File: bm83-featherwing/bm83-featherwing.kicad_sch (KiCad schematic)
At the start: 19 parts, among them J1 TOP, J2 BOT, J3 DX07S016JA1R1500, SW1 Reset Switch, SW2 Power Switch, U1 BM83SM1-00AA

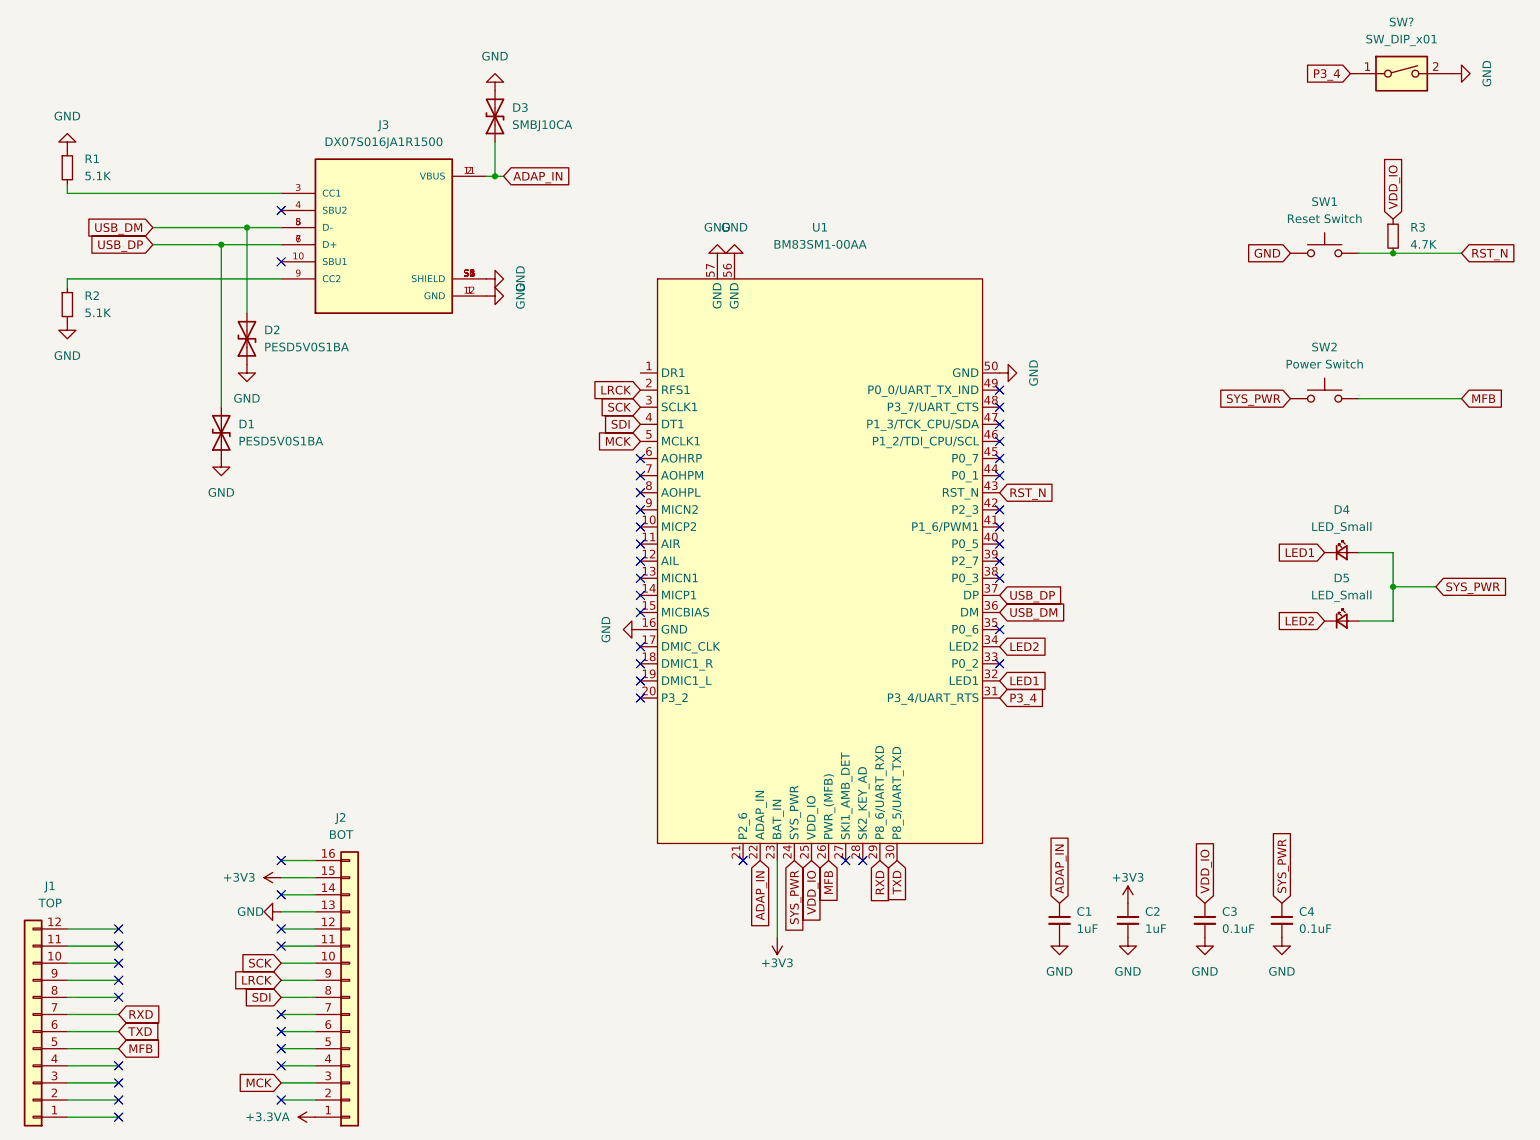
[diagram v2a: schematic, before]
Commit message: BM83 board first route. Needs labelling
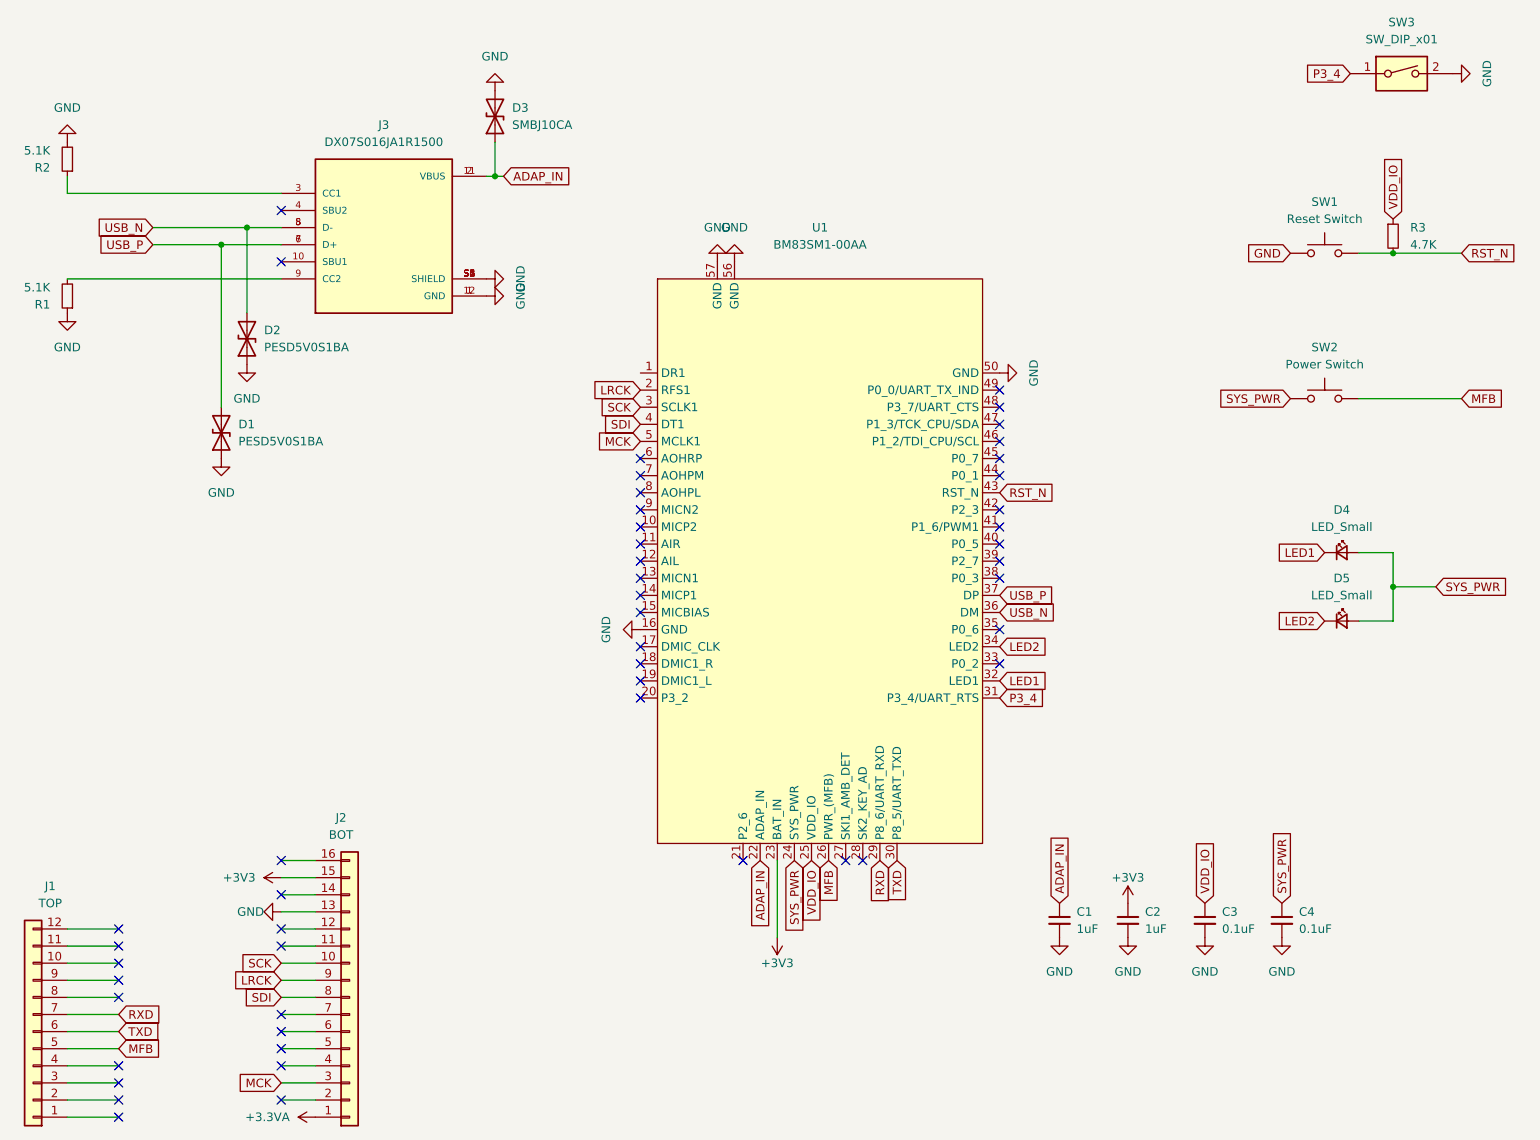
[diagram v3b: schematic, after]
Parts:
- SW3: renamed from SW?; footprint (none) -> Button_Switch_SMD:SW_DIP_SPSTx01_Slide_Copal_CHS-01A_W5.08mm_P1.27mm_JPin
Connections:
- net at J3.3 (CC1): now also R2.1; no longer R1.2
- net at J3.9 (CC2): now also R1.2; no longer R2.1
- net USB_DM renamed USB_N
- net USB_DP renamed USB_P
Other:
- moved on the sheet: R1, R2
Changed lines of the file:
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@@
-(kicad_sch (version 20210126) (generator eeschema)
+(kicad_sch (version 20210406) (generator eeschema)
   (paper "A4")
   (junction (at 55.88 53.34) (diameter 0.9144) (color 0 0 0 0))
@@
   (no_connect (at 171.45 110.49))
   (no_connect (at 171.45 115.57))
-  (wire (pts (xy 33.02 44.45) (xy 33.02 45.72))
+  (wire (pts (xy 33.02 43.18) (xy 33.02 45.72))
     (stroke (width 0) (type solid) (color 0 0 0 0))
   )
@@
     (stroke (width 0) (type solid) (color 0 0 0 0))
   )
-  (wire (pts (xy 33.02 58.42) (xy 33.02 59.69))
-    (stroke (width 0) (type solid) (color 0 0 0 0))
-  )
   (wire (pts (xy 33.02 58.42) (xy 64.77 58.42))
     (stroke (width 0) (type solid) (color 0 0 0 0))
@@
     )
   )
-  (global_label "USB_DM" (shape input) (at 45.72 50.8 180)
+  (global_label "USB_N" (shape input) (at 45.72 50.8 180)
     (effects (font (size 1.27 1.27)) (justify right))
     (property "Intersheet References" "${INTERSHEET_REFS}" (id 0) (at 35.8079 50.8794 0)
@@
     )
   )
-  (global_label "USB_DP" (shape input) (at 45.72 53.34 180)
+  (global_label "USB_P" (shape input) (at 45.72 53.34 180)
     (effects (font (size 1.27 1.27)) (justify right))
     (property "Intersheet References" "${INTERSHEET_REFS}" (id 0) (at 35.9893 53.4194 0)
@@
     )
   )
-  (global_label "USB_DP" (shape input) (at 171.45 105.41 0)
+  (global_label "USB_P" (shape input) (at 171.45 105.41 0)
     (effects (font (size 1.27 1.27)) (justify left))
     (property "Intersheet References" "${INTERSHEET_REFS}" (id 0) (at 181.1807 105.3306 0)
@@
     )
   )
-  (global_label "USB_DM" (shape input) (at 171.45 107.95 0)
+  (global_label "USB_N" (shape input) (at 171.45 107.95 0)
     (effects (font (size 1.27 1.27)) (justify left))
     (property "Intersheet References" "${INTERSHEET_REFS}" (id 0) (at 181.3621 107.8706 0)
@@
     (pin "1")
   )
-  (symbol (lib_id "power:GND") (at 33.02 39.37 180) (unit 1)
-    (in_bom yes) (on_board yes)
-    (property "Reference" "#PWR0118" (id 0) (at 33.02 33.02 0)
-      (effects (font (size 1.27 1.27)) hide)
-    )
-    (property "Value" "GND" (id 1) (at 33.02 34.29 0))
-    (property "Footprint" "" (id 2) (at 33.02 39.37 0)
-      (effects (font (size 1.27 1.27)) hide)
-    )
-    (property "Datasheet" "" (id 3) (at 33.02 39.37 0)
-      (effects (font (size 1.27 1.27)) hide)
-    )
-    (pin "1")
-  )
-  (symbol (lib_id "power:GND") (at 33.02 64.77 0) (unit 1)
-    (in_bom yes) (on_board yes)
-    (property "Reference" "#PWR0117" (id 0) (at 33.02 71.12 0)
-      (effects (font (size 1.27 1.27)) hide)
-    )
-    (property "Value" "GND" (id 1) (at 33.02 69.85 0))
-    (property "Footprint" "" (id 2) (at 33.02 64.77 0)
-      (effects (font (size 1.27 1.27)) hide)
-    )
-    (property "Datasheet" "" (id 3) (at 33.02 64.77 0)
+  (symbol (lib_id "power:GND") (at 33.02 38.1 180) (unit 1)
+    (in_bom yes) (on_board yes)
+    (property "Reference" "#PWR0117" (id 0) (at 33.02 31.75 0)
+      (effects (font (size 1.27 1.27)) hide)
+    )
+    (property "Value" "GND" (id 1) (at 33.02 33.02 0))
+    (property "Footprint" "" (id 2) (at 33.02 38.1 0)
+      (effects (font (size 1.27 1.27)) hide)
+    )
+    (property "Datasheet" "" (id 3) (at 33.02 38.1 0)
+      (effects (font (size 1.27 1.27)) hide)
+    )
+    (pin "1")
+  )
+  (symbol (lib_id "power:GND") (at 33.02 63.5 0) (unit 1)
+    (in_bom yes) (on_board yes)
+    (property "Reference" "#PWR0118" (id 0) (at 33.02 69.85 0)
+      (effects (font (size 1.27 1.27)) hide)
+    )
+    (property "Value" "GND" (id 1) (at 33.02 68.58 0))
+    (property "Footprint" "" (id 2) (at 33.02 63.5 0)
+      (effects (font (size 1.27 1.27)) hide)
+    )
+    (property "Datasheet" "" (id 3) (at 33.02 63.5 0)
       (effects (font (size 1.27 1.27)) hide)
     )
@@
     (pin "1")
   )
-  (symbol (lib_id "Device:R_Small") (at 33.02 41.91 0) (unit 1)
-    (in_bom yes) (on_board yes)
-    (property "Reference" "R1" (id 0) (at 35.56 40.64 0)
-      (effects (font (size 1.27 1.27)) (justify left))
-    )
-    (property "Value" "5.1K" (id 1) (at 35.56 43.18 0)
-      (effects (font (size 1.27 1.27)) (justify left))
-    )
-    (property "Footprint" "Resistor_SMD:R_0805_2012Metric_Pad1.20x1.40mm_HandSolder" (id 2) (at 33.02 41.91 0)
-      (effects (font (size 1.27 1.27)) hide)
-    )
-    (property "Datasheet" "~" (id 3) (at 33.02 41.91 0)
-      (effects (font (size 1.27 1.27)) hide)
-    )
-    (pin "1")
-    (pin "2")
-  )
-  (symbol (lib_id "Device:R_Small") (at 33.02 62.23 0) (unit 1)
-    (in_bom yes) (on_board yes)
-    (property "Reference" "R2" (id 0) (at 35.56 60.96 0)
-      (effects (font (size 1.27 1.27)) (justify left))
-    )
-    (property "Value" "5.1K" (id 1) (at 35.56 63.5 0)
-      (effects (font (size 1.27 1.27)) (justify left))
-    )
-    (property "Footprint" "Resistor_SMD:R_0805_2012Metric_Pad1.20x1.40mm_HandSolder" (id 2) (at 33.02 62.23 0)
-      (effects (font (size 1.27 1.27)) hide)
-    )
-    (property "Datasheet" "~" (id 3) (at 33.02 62.23 0)
+  (symbol (lib_id "Device:R_Small") (at 33.02 40.64 180) (unit 1)
+    (in_bom yes) (on_board yes)
+    (property "Reference" "R2" (id 0) (at 30.48 41.91 0)
+      (effects (font (size 1.27 1.27)) (justify left))
+    )
+    (property "Value" "5.1K" (id 1) (at 30.48 39.37 0)
+      (effects (font (size 1.27 1.27)) (justify left))
+    )
+    (property "Footprint" "Resistor_SMD:R_0805_2012Metric_Pad1.20x1.40mm_HandSolder" (id 2) (at 33.02 40.64 0)
+      (effects (font (size 1.27 1.27)) hide)
+    )
+    (property "Datasheet" "~" (id 3) (at 33.02 40.64 0)
+      (effects (font (size 1.27 1.27)) hide)
+    )
+    (pin "1")
+    (pin "2")
+  )
+  (symbol (lib_id "Device:R_Small") (at 33.02 60.96 180) (unit 1)
+    (in_bom yes) (on_board yes)
+    (property "Reference" "R1" (id 0) (at 30.48 62.23 0)
+      (effects (font (size 1.27 1.27)) (justify left))
+    )
+    (property "Value" "5.1K" (id 1) (at 30.48 59.69 0)
+      (effects (font (size 1.27 1.27)) (justify left))
+    )
+    (property "Footprint" "Resistor_SMD:R_0805_2012Metric_Pad1.20x1.40mm_HandSolder" (id 2) (at 33.02 60.96 0)
+      (effects (font (size 1.27 1.27)) hide)
+    )
+    (property "Datasheet" "~" (id 3) (at 33.02 60.96 0)
       (effects (font (size 1.27 1.27)) hide)
     )
@@
   (symbol (lib_id "Switch:SW_DIP_x01") (at 231.14 27.94 0) (unit 1)
     (in_bom yes) (on_board yes)
-    (property "Reference" "SW?" (id 0) (at 231.14 20.32 0))
+    (property "Reference" "SW3" (id 0) (at 231.14 20.32 0))
     (property "Value" "SW_DIP_x01" (id 1) (at 231.14 22.86 0))
-    (property "Footprint" "" (id 2) (at 231.14 27.94 0)
+    (property "Footprint" "Button_Switch_SMD:SW_DIP_SPSTx01_Slide_Copal_CHS-01A_W5.08mm_P1.27mm_JPin" (id 2) (at 231.14 27.94 0)
       (effects (font (size 1.27 1.27)) hide)
     )
@@
     )
     (path "/5b302fa4-059a-4878-8524-670aea735c7c"
-      (reference "SW?") (unit 1) (value "SW_DIP_x01") (footprint "")
+      (reference "SW3") (unit 1) (value "SW_DIP_x01") (footprint "Button_Switch_SMD:SW_DIP_SPSTx01_Slide_Copal_CHS-01A_W5.08mm_P1.27mm_JPin")
     )
     (path "/bfaec5dd-dca1-4ce3-a1de-1f59bdc18b31"
